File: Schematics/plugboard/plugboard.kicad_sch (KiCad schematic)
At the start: 35 parts, among them J1 Conn_01x01_Socket, J10 Conn_01x01_Socket, J11 Conn_01x01_Socket, J12 Conn_01x01_Socket, J13 Conn_01x01_Socket, J14 Conn_01x01_Socket, J15 Conn_01x01_Socket, J16 Conn_01x01_Socket, J17 Conn_01x01_Socket, J18 Conn_01x01_Socket, J19 Conn_01x01_Socket, J2 Conn_01x01_Socket, J20 Conn_01x01_Socket, J21 Conn_01x01_Socket, J22 Conn_01x01_Socket, J23 Conn_01x01_Socket, J24 Conn_01x01_Socket, J25 Conn_01x01_Socket, J26 Conn_01x01_Socket, J27 Conn_01x04, J3 Conn_01x01_Socket, J4 Conn_01x01_Socket, J5 Conn_01x01_Socket, J6 Conn_01x01_Socket, J7 Conn_01x01_Socket, J8 Conn_01x01_Socket, J9 Conn_01x01_Socket, U1 MCP23017_SP, U2 MCP23017_SP

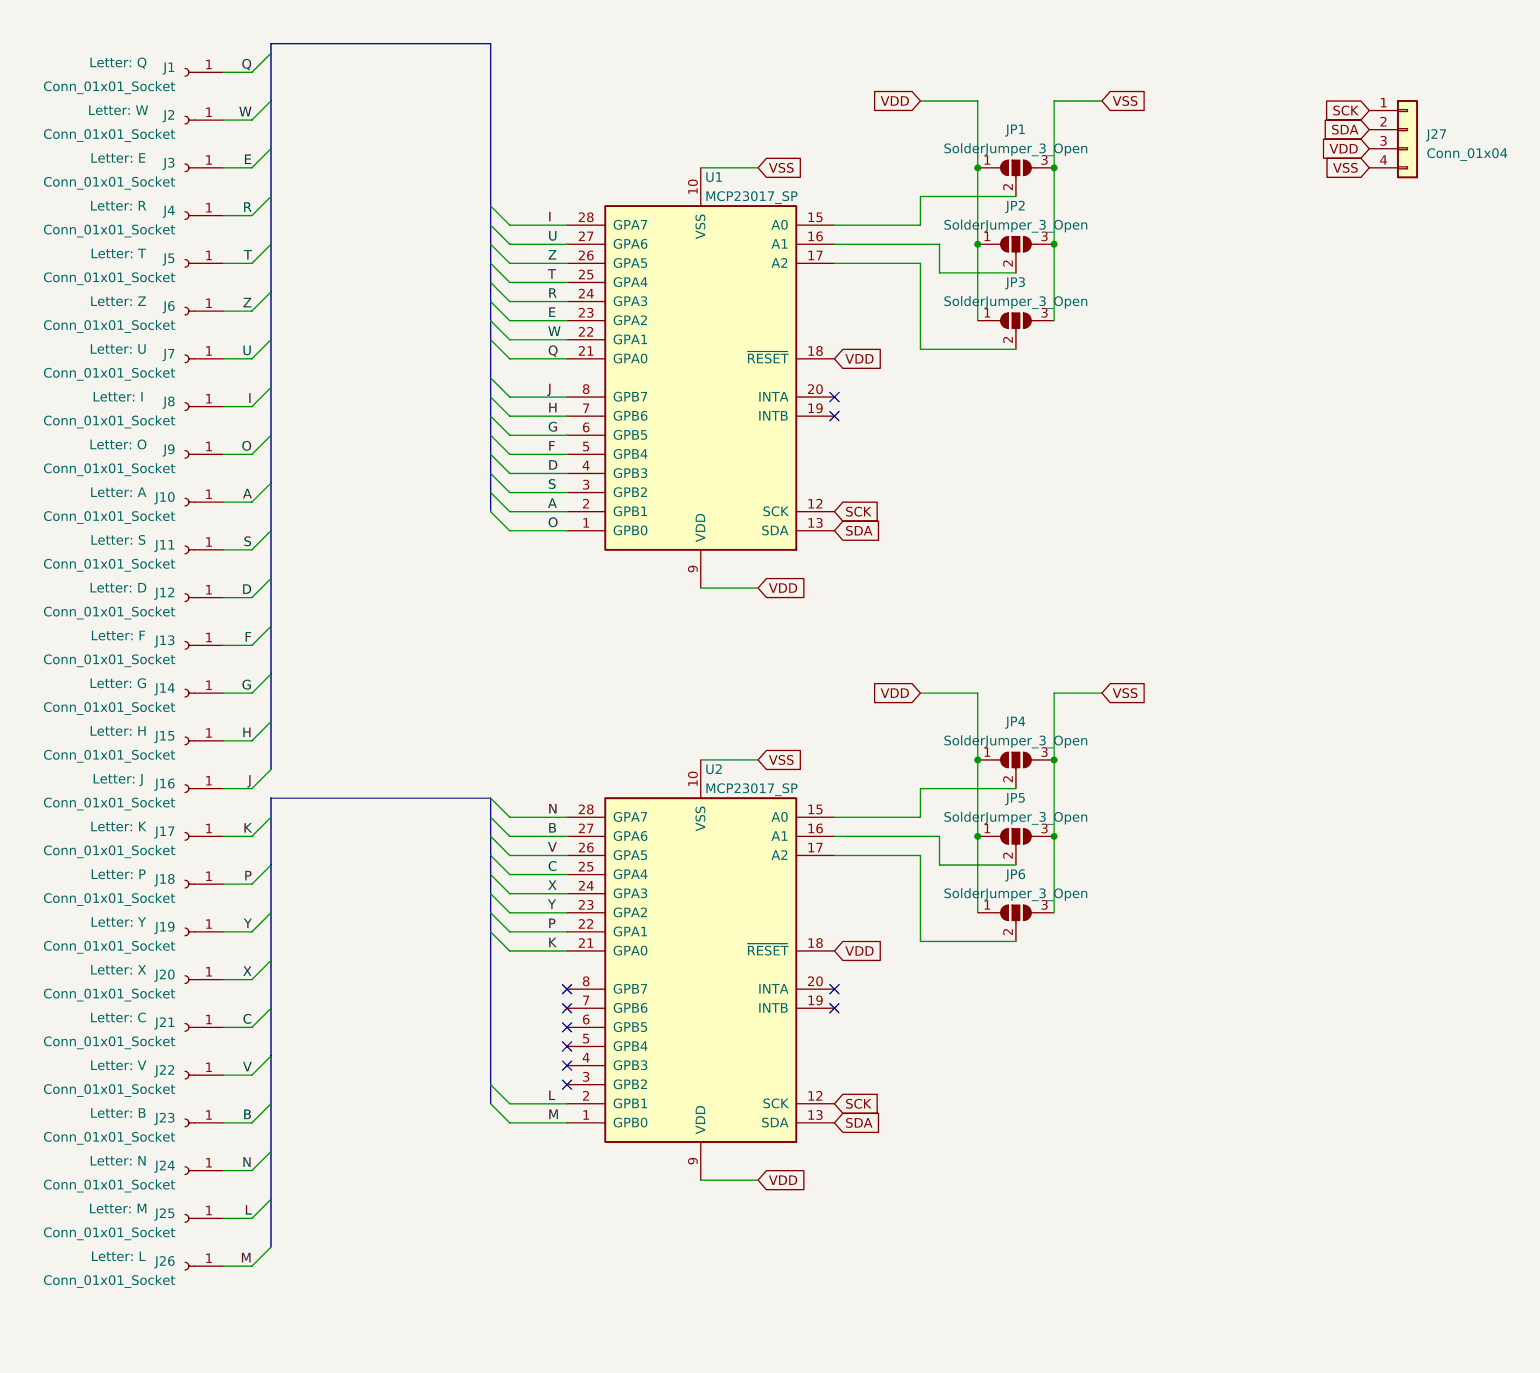
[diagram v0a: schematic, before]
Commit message: Plugboard PCB design done and send for manufacturing + a few edits
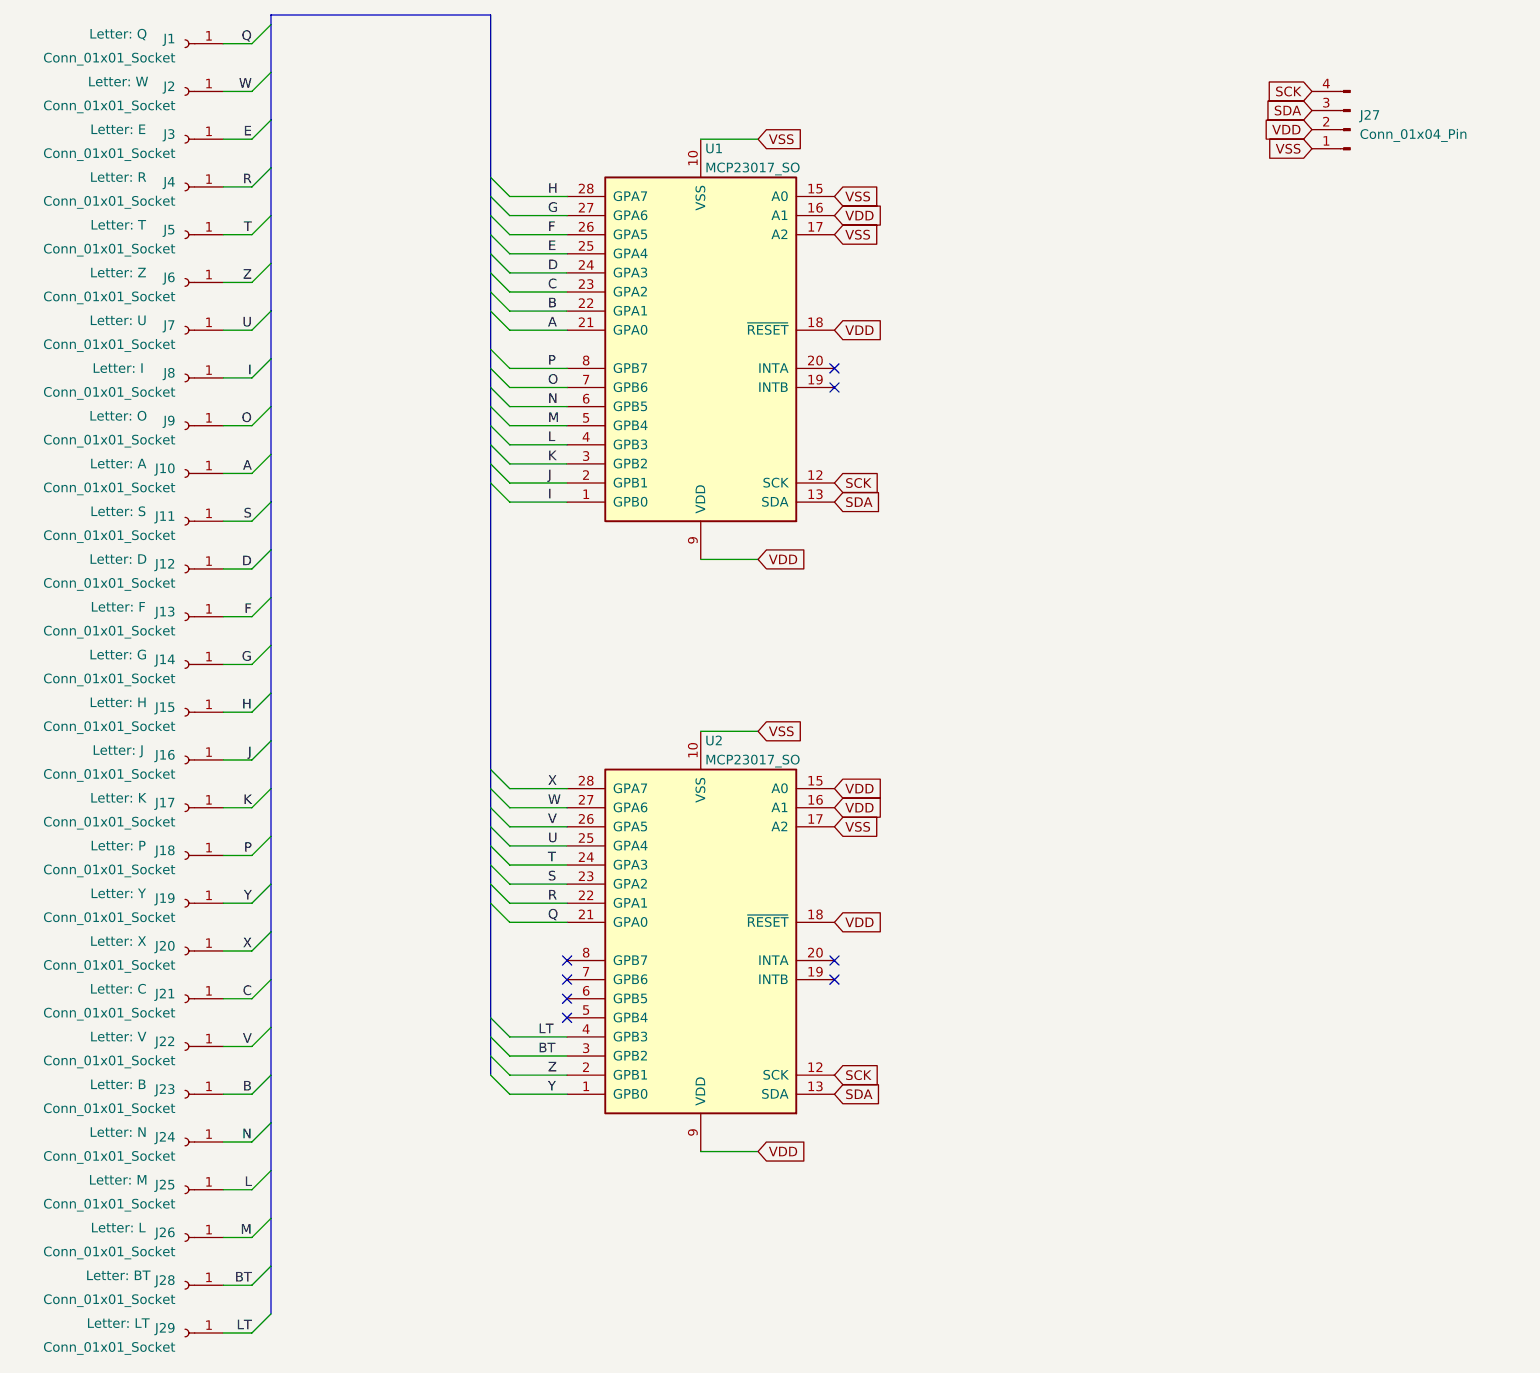
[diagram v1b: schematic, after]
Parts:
- removed JP1, JP2, JP3, JP4, JP5, JP6: SolderJumper_3_Open, SolderJumper-3_P1.3mm_Open_RoundedPad1.0x1.5mm_NumberLabels, symbol Jumper:SolderJumper_3_Open
- added J28, J29: Conn_01x01_Socket, user_global_footprints:plugboard_test_socket, symbol Connector:Conn_01x01_Socket
- J1, J10, J11, J12, J13, J14, J15, J16, J17, J18, J19, J2, J20, J21, J22, J23, J24, J25, J26, J3, J4, J5, J6, J7, J8, J9: footprint Connector:Banana_Jack_1Pin -> user_global_footprints:plugboard_socket
- J27: value Conn_01x04 -> Conn_01x04_Pin; footprint Connector_PinHeader_2.54mm:PinHeader_1x04_P2.54mm_Vertical -> user_global_footprints:PinHeader_1x04_P2.54mm_Vertical_SLIM; symbol Connector_Generic:Conn_01x04 -> Connector:Conn_01x04_Pin; Check_prices (none) -> https://www.snapeda.com/parts/TSM-104-01-T-SH-A/Samtec+Inc.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; DigiKey_Part_Number (none) -> TSM-104-01-T-SH-A-ND; MANUFACTURER (none) -> Samtec; MF (none) -> Samtec Inc.; MP (none) -> TSM-104-01-T-SH-A; PARTREV (none) -> R; Package (none) -> None; STANDARD (none) -> Manufacturer Recommendations; SnapEDA_Link (none) -> https://www.snapeda.com/parts/TSM-104-01-T-SH-A/Samtec+Inc.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
- U1, U2: value MCP23017_SP -> MCP23017_SO; footprint Package_DIP:DIP-28_W7.62mm -> user_global_footprints:SOIC-28W_7.5x17.9mm_P1.27mm_long_pads; symbol Interface_Expansion:MCP23017_SP -> Interface_Expansion:MCP23017_SO
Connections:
- net A: now also U1.21 (GPA0); no longer U1.2 (GPB1)
- net B: now also U1.22 (GPA1); no longer U2.27 (GPA6)
- net C: now also U1.23 (GPA2); no longer U2.25 (GPA4)
- net D: now also U1.24 (GPA3); no longer U1.4 (GPB3)
- net E: now also U1.25 (GPA4); no longer U1.23 (GPA2)
- net F: now also U1.26 (GPA5); no longer U1.5 (GPB4)
- net G: now also U1.27 (GPA6); no longer U1.6 (GPB5)
- net H: now also U1.28 (GPA7); no longer U1.7 (GPB6)
- net I: now also U1.1 (GPB0); no longer U1.28 (GPA7)
- net J: now also U1.2 (GPB1); no longer U1.8 (GPB7)
- net K: now also U1.3 (GPB2); no longer U2.21 (GPA0)
- net L: now also U1.4 (GPB3); no longer U2.2 (GPB1)
- net M: now also U1.5 (GPB4); no longer U2.1 (GPB0)
- net N: now also U1.6 (GPB5); no longer U2.28 (GPA7)
- net O: now also U1.7 (GPB6); no longer U1.1 (GPB0)
- net P: now also U1.8 (GPB7); no longer U2.22 (GPA1)
- net Q: now also U2.21 (GPA0); no longer U1.21 (GPA0)
- net R: now also U2.22 (GPA1); no longer U1.24 (GPA3)
- net S: now also U2.23 (GPA2); no longer U1.3 (GPB2)
- net SCK: now also J27.4 (Pin_4); no longer J27.1 (Pin_1)
- net SDA: now also J27.3 (Pin_3); no longer J27.2 (Pin_2)
- net T: now also U2.24 (GPA3); no longer U1.25 (GPA4)
- net U: now also U2.25 (GPA4); no longer U1.27 (GPA6)
- net VDD: now also J27.2 (Pin_2), U1.16 (A1), U2.15 (A0), U2.16 (A1); no longer J27.3 (Pin_3)
- net VSS: now also J27.1 (Pin_1), U1.15 (A0), U1.17 (A2), U2.17 (A2); no longer J27.4 (Pin_4)
- net W: now also U2.27 (GPA6); no longer U1.22 (GPA1)
- net X: now also U2.28 (GPA7); no longer U2.24 (GPA3)
- net Y: now also U2.1 (GPB0); no longer U2.23 (GPA2)
- net Z: now also U2.2 (GPB1); no longer U1.26 (GPA5)
- net BT: now reaches U2.3 (GPB2)
- net BT: now also J28.1 (Pin_1)
- net LT: now reaches U2.4 (GPB3)
- net LT: now also J29.1 (Pin_1)
- no-connect marks 10 -> 8
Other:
- moved on the sheet: J1, J10, J11, J12, J13, J14, J15, J16, J17, J18, J19, J2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
